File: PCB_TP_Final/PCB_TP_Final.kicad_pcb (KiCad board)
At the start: 2 copper layers, 71 x 135 mm, 20 parts, among them CN10 Conn_02x17_Odd_Even, CN7 Conn_02x10_Odd_Even, CN8 Conn_02x08_Odd_Even, CN9 Conn_02x15_Odd_Even, J1 Conn_01x09, M1 POWER_MB_V2, SW1 SW_Push, U1 NODEMCU_ESP12

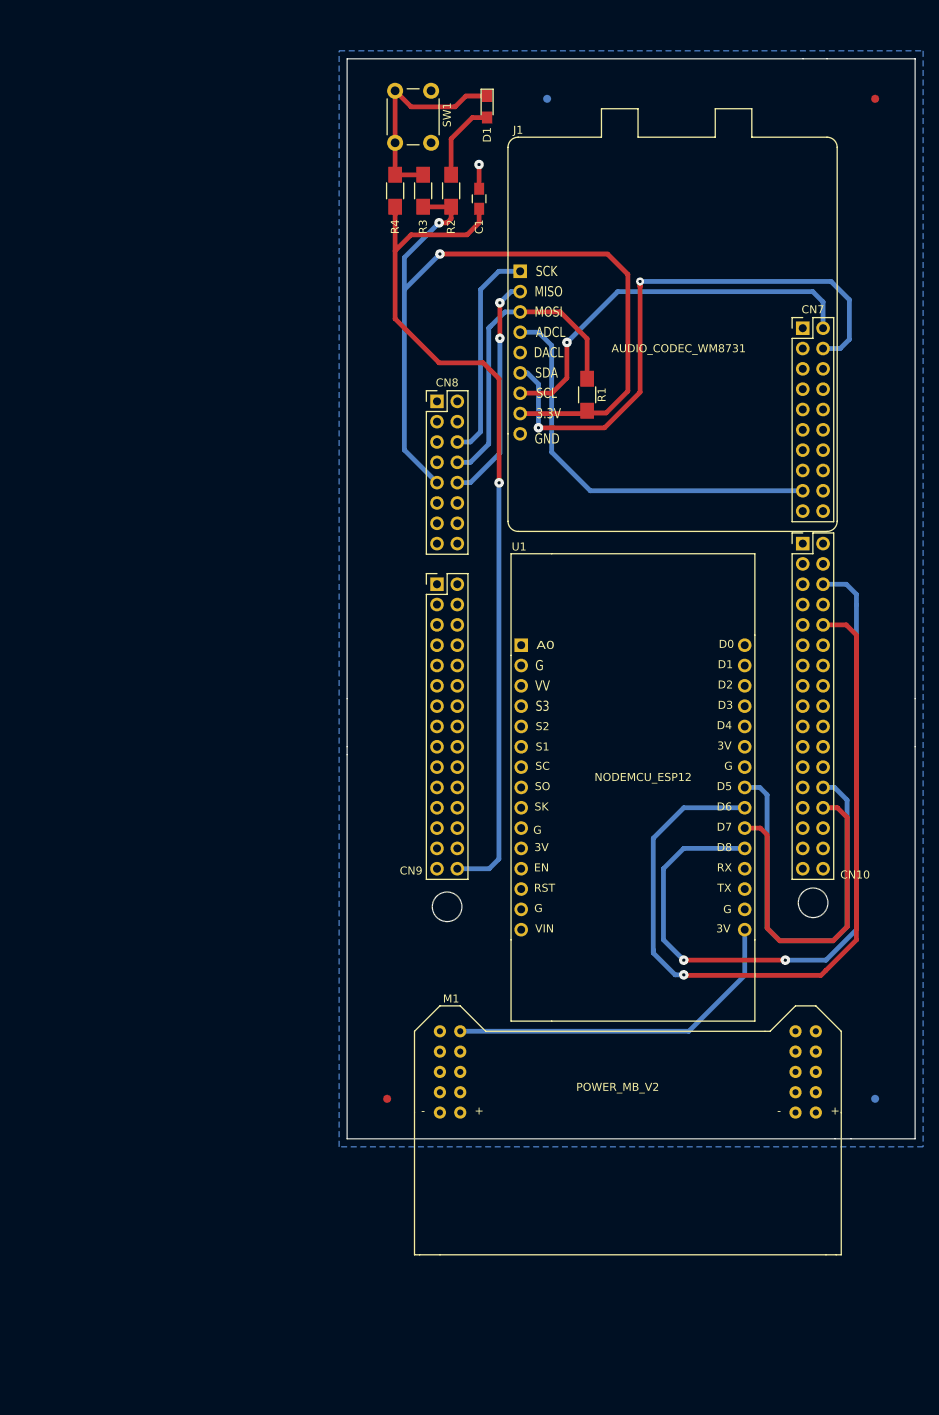
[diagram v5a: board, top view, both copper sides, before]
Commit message: Se agregaron correcciones sugeridas
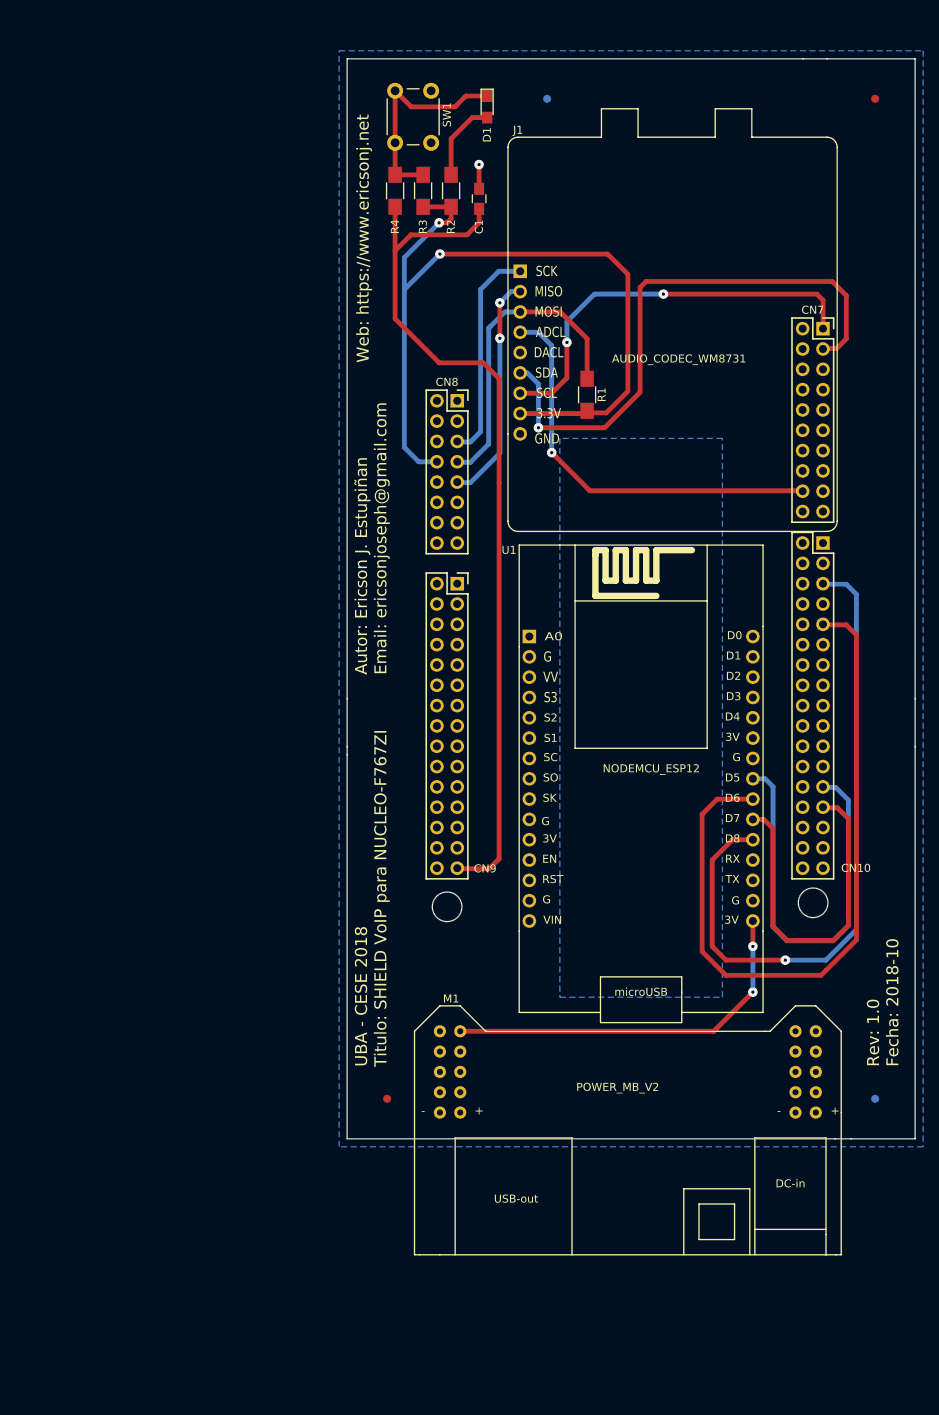
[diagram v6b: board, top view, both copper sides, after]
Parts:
- CN10: footprint Connector_PinHeader_2.54mm:PinHeader_2x17_P2.54mm_Vertical -> Pin_Headers:Pin_Header_Straight_2x17_Pitch2.54mm; moved to B.Cu
- CN7: footprint Connector_PinHeader_2.54mm:PinHeader_2x10_P2.54mm_Vertical -> Pin_Headers:Pin_Header_Straight_2x10_Pitch2.54mm; moved to B.Cu
- CN8: footprint Connector_PinHeader_2.54mm:PinHeader_2x08_P2.54mm_Vertical -> Pin_Headers:Pin_Header_Straight_2x08_Pitch2.54mm; moved to B.Cu
- CN9: footprint Connector_PinHeader_2.54mm:PinHeader_2x15_P2.54mm_Vertical -> Pin_Headers:Pin_Header_Straight_2x15_Pitch2.54mm; moved to B.Cu
- moved CN9 2.53 mm to (117.3, 88.6), turned to 180 degrees
- moved CN10 2.53 mm to (163.0, 83.5), turned to 180 degrees
- moved CN8 2.53 mm to (117.3, 65.8), turned to 180 degrees
- moved CN7 2.53 mm to (163.0, 56.7), turned to 180 degrees
- moved U1 1.15 mm to (140.9, 113.0)
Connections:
- CN10 pad 10: /NODEMCU_ESP12/HMISO -> Net-(CN10-Pad10)
- CN10 pad 25: Net-(CN10-Pad25) -> /NODEMCU_ESP12/HSCLK
- CN10 pad 26: /NODEMCU_ESP12/HSCLK -> Net-(CN10-Pad26)
- CN10 pad 27: Net-(CN10-Pad27) -> /NODEMCU_ESP12/HMOSI
- CN10 pad 28: /NODEMCU_ESP12/HMOSI -> Net-(CN10-Pad28)
- CN10 pad 5: Net-(CN10-Pad5) -> /NODEMCU_ESP12/HCS
- CN10 pad 6: /NODEMCU_ESP12/HCS -> Net-(CN10-Pad6)
- CN10 pad 9: Net-(CN10-Pad9) -> /NODEMCU_ESP12/HMISO
- CN7 pad 1: Net-(CN7-Pad1) -> /AUDIO_CODEC/SCL
- CN7 pad 17: /AUDIO_CODEC/ADCL -> Net-(CN7-Pad17)
- CN7 pad 18: Net-(CN7-Pad18) -> /AUDIO_CODEC/ADCL
- CN7 pad 2: /AUDIO_CODEC/SCL -> Net-(CN7-Pad2)
- CN7 pad 3: Net-(CN7-Pad3) -> /AUDIO_CODEC/SDA
- CN7 pad 4: /AUDIO_CODEC/SDA -> Net-(CN7-Pad4)
- CN8 pad 10: /AUDIO_CODEC/MISO -> Net-(CN8-Pad10)
- CN8 pad 11: GND -> Net-(CN8-Pad11)
- CN8 pad 12: Net-(CN8-Pad12) -> GND
- CN8 pad 13: GND -> Net-(CN8-Pad13)
- CN8 pad 14: Net-(CN8-Pad14) -> GND
- CN8 pad 5: Net-(CN8-Pad5) -> /AUDIO_CODEC/SCK
- CN8 pad 6: /AUDIO_CODEC/SCK -> Net-(CN8-Pad6)
- CN8 pad 7: Net-(CN8-Pad7) -> /AUDIO_CODEC/MOSI
- CN8 pad 8: /AUDIO_CODEC/MOSI -> +3.3VA
- CN8 pad 9: 3.3VB -> /AUDIO_CODEC/MISO
- CN9 pad 11: Net-(CN9-Pad11) -> GND
- CN9 pad 12: GND -> Net-(CN9-Pad12)
- CN9 pad 29: Net-(CN9-Pad29) -> /TalkButton/talk
- CN9 pad 30: /TalkButton/talk -> Net-(CN9-Pad30)
- J1 pad 8: 3.3VB -> +3.3VA
- R1 pad 2: 3.3VB -> +3.3VA
- R2 pad 2: 3.3VB -> +3.3VA
- R3 pad 2: 3.3VB -> +3.3VA
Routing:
- net 3.3VB: track 103.1 -> 0.00 mm, vias 2 -> 0
- net +3.3VA: track 0.00 -> 102.0 mm, vias 0 -> 2
- net /NODEMCU_ESP12/HCS: track 93.5 -> 83.9 mm, vias 2 -> 1
- net /NODEMCU_ESP12/HMISO: track 98.5 -> 89.5 mm, vias 1 -> 0
- net +3V3: track 44.2 -> 47.5 mm, vias 0 -> 2
- net /AUDIO_CODEC/SDA: track 73.2 -> 71.6 mm, vias 2 -> 1
- net /AUDIO_CODEC/SCL: track 49.5 -> 50.9 mm, vias 1 -> 2
- net /TalkButton/talk: track 110.6 -> 110.5 mm, vias 1 -> 0
- net /AUDIO_CODEC/ADCL: track 51.3 -> 51.4 mm, vias 0 -> 1
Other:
- board text added: "Autor: Ericson J. Estupiñan Email: ericsonjoseph@gmail.com"
- board text added: "Rev: 1.0 Fecha: 2018-10"
- board text added: "UBA - CESE 2018 Titulo: SHIELD VoIP para NUCLEO-F767ZI"
- board text added: "Web: https://www.ericsonj.net"

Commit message: Versión lista para revisión
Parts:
- moved F2 0.07 mm to (128.4, 28.0)
- moved F4 0.05 mm to (169.5, 28.0)
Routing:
- net /AUDIO_CODEC/MISO: track 28.8 -> 29.2 mm, vias 2 -> 1
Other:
- board text added: "Minimos (Mayer 5 mils): Grillas: 0.1270mm, 0.5mm, 0.6350mm, 2.54mm Via 1.2mm, 0.6mm: Margen: 0.4mm Pista: 0.6mm Dist. a borde: 0.6mm Terminación: HASL"
- board text removed: "Minimos (Mayer 100 mils): Grillas: 0.1270mm, 0.5mm, 0.6350mm, 2.54mm Via 1.2mm, 0.6mm: Margen: 0.4mm Pista: 0.6mm Dist. a borde: 0.6mm Terminación: HASL"
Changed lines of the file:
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@@
     (area 103.449999 22.949999 174.550001 158.050001)
     (thickness 1.6)
-    (drawings 52)
+    (drawings 51)
     (tracks 156)
     (zones 0)
@@
   )
   (module Fiducials:Fiducial_1mm_Dia_2.54mm_Outer_CopperBottom (layer F.Cu)
-    (at 128.5 28)
+    (at 128.439 28.032)
     (descr "Circular Fiducial, 1mm bare copper bottom; 2.54mm keepout")
     (tags marker)
@@
   )
   (module Fiducials:Fiducial_1mm_Dia_2.54mm_Outer_CopperTop (layer F.Cu)
-    (at 169.5 28)
+    (at 169.46 28.032)
     (descr "Circular Fiducial, 1mm bare copper top; 2.54mm keepout")
     (tags marker)
@@
       (effects (font (size 1 1) (thickness 0.15)))
     )
-    (fp_text value Conn_02x08_Odd_Even (at 1.27 -20.11 180) (layer B.Fab)
+    (fp_text value Conn_02x08_Odd_Even (at 5.334 -9.144 270) (layer B.Fab)
       (effects (font (size 1 1) (thickness 0.15)) (justify mirror))
     )
@@
       (effects (font (size 1 1) (thickness 0.15)))
     )
-    (fp_text value Conn_02x15_Odd_Even (at 1.27 -37.89 180) (layer B.Fab)
+    (fp_text value Conn_02x15_Odd_Even (at 5.334 -17.018 270) (layer B.Fab)
       (effects (font (size 1 1) (thickness 0.15)) (justify mirror))
     )
@@
       (effects (font (size 1 1) (thickness 0.15)))
     )
-    (fp_text value Conn_02x10_Odd_Even (at 1.27 -25.19 180) (layer B.Fab)
+    (fp_text value Conn_02x10_Odd_Even (at 5.334 -10.795 270) (layer B.Fab)
       (effects (font (size 1 1) (thickness 0.15)) (justify mirror))
     )
@@
       (effects (font (size 1 1) (thickness 0.15)))
     )
-    (fp_text value Conn_02x17_Odd_Even (at 1.27 -42.97 180) (layer B.Fab)
+    (fp_text value Conn_02x17_Odd_Even (at 5.334 -14.732 270) (layer B.Fab)
       (effects (font (size 1 1) (thickness 0.15)) (justify mirror))
     )
@@
   (gr_line (start 115.993 64.4175) (end 115.993 67.021) (angle 90) (layer F.SilkS) (width 0.2))
   (gr_line (start 113.3895 64.4175) (end 115.993 64.4175) (angle 90) (layer F.SilkS) (width 0.2))
-  (dimension 48.26 (width 0.3) (layer Dwgs.User)
-    (gr_text "48.260 mm" (at 138.726 136.363) (layer Dwgs.User)
-      (effects (font (size 1.5 1.5) (thickness 0.3)))
-    )
-    (feature1 (pts (xy 162.983 124.298) (xy 162.983 140.968)))
-    (feature2 (pts (xy 114.723 124.298) (xy 114.723 140.968)))
-    (crossbar (pts (xy 114.723 138.268) (xy 162.983 138.268)))
-    (arrow1a (pts (xy 162.983 138.268) (xy 161.856496 138.854421)))
-    (arrow1b (pts (xy 162.983 138.268) (xy 161.856496 137.681579)))
-    (arrow2a (pts (xy 114.723 138.268) (xy 115.849504 138.854421)))
-    (arrow2b (pts (xy 114.723 138.268) (xy 115.849504 137.681579)))
-  )
   (gr_text "Rev: 1.0\nFecha: 2018-10" (at 170.5 149 90) (layer F.SilkS)
     (effects (font (size 1.5 1.5) (thickness 0.3)) (justify left))
@@
     (effects (font (size 1.5 1.5) (thickness 0.3)) (justify left))
   )
-  (gr_text "Minimos (Mayer 100 mils):\nGrillas: 0.1270mm, 0.5mm, 0.6350mm, 2.54mm\nVia 1.2mm, 0.6mm:\nMargen: 0.4mm\nPista: 0.6mm\nDist. a borde: 0.6mm\nTerminación: HASL" (at 177.2705 31.6515) (layer Dwgs.User)
+  (gr_text "Minimos (Mayer 5 mils):\nGrillas: 0.1270mm, 0.5mm, 0.6350mm, 2.54mm\nVia 1.2mm, 0.6mm:\nMargen: 0.4mm\nPista: 0.6mm\nDist. a borde: 0.6mm\nTerminación: HASL" (at 177.2705 31.6515) (layer Dwgs.User)
     (effects (font (size 1.5 1.5) (thickness 0.3)) (justify left))
   )
@@
   (via (at 154.22 139.665) (size 1.2) (drill 0.4) (layers F.Cu B.Cu) (net 79))
   (segment (start 149.325 144.56) (end 154.22 139.665) (width 0.6) (layer F.Cu) (net 79))
-  (segment (start 123.99 52.104) (end 125.133 52.104) (width 0.6) (layer B.Cu) (net 80))
+  (segment (start 122.593 53.501) (end 122.593 52.928) (width 0.6) (layer F.Cu) (net 80))
+  (via (at 122.597 57.9405) (size 1.2) (drill 0.4) (layers F.Cu B.Cu) (net 80))
+  (segment (start 122.597 57.9405) (end 122.593 57.9365) (width 0.6) (layer F.Cu) (net 80))
+  (segment (start 122.593 53.501) (end 122.593 57.9365) (width 0.6) (layer F.Cu) (net 80))
+  (segment (start 123.417 52.104) (end 125.133 52.104) (width 0.6) (layer F.Cu) (net 80))
+  (segment (start 122.593 52.928) (end 123.417 52.104) (width 0.6) (layer F.Cu) (net 80))
   (segment (start 122.597 57.9405) (end 122.597 72.293) (width 0.6) (layer B.Cu) (net 80))
   (segment (start 118.91 75.98) (end 117.27424 75.98) (width 0.6) (layer B.Cu) (net 80))
   (segment (start 122.597 72.293) (end 118.91 75.98) (width 0.6) (layer B.Cu) (net 80))
   (segment (start 122.597 57.9405) (end 122.550002 57.987498) (width 0.6) (layer B.Cu) (net 80))
-  (via (at 122.597 57.9405) (size 1.2) (drill 0.4) (layers F.Cu B.Cu) (net 80))
-  (segment (start 122.593 57.9365) (end 122.597 57.9405) (width 0.6) (layer F.Cu) (net 80))
-  (segment (start 122.593 53.501) (end 122.593 57.9365) (width 0.6) (layer F.Cu) (net 80))
-  (segment (start 122.593 53.501) (end 123.99 52.104) (width 0.6) (layer B.Cu) (net 80))
-  (via (at 122.593 53.501) (size 1.2) (drill 0.4) (layers F.Cu B.Cu) (net 80))
   (segment (start 151.68 120.615) (end 154.22 120.615) (width 0.6) (layer F.Cu) (net 111))
   (segment (start 149.14 123.155) (end 151.68 120.615) (width 0.6) (layer F.Cu) (net 111))

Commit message: para fabricar
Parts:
- added R5: 10K, Resistors_SMD:R_1206_HandSoldering, F.Cu at (146.7, 122.0)
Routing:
- net /NODEMCU_ESP12/HMOSI: track 43.2 -> 52.4 mm
- net /NODEMCU_ESP12/HMISO: track 89.5 -> 94.7 mm
- net GND: track 3.03 -> 7.25 mm, vias 1 -> 2
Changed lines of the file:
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@@
 (kicad_pcb (version 4) (host pcbnew 4.0.7)
   (general
-    (links 31)
+    (links 33)
     (no_connects 0)
-    (area 103.449999 22.949999 174.550001 158.050001)
+    (area 88.435716 22 232.270495 176.700001)
     (thickness 1.6)
     (drawings 51)
-    (tracks 156)
+    (tracks 164)
     (zones 0)
-    (modules 20)
+    (modules 21)
     (nets 133)
   )
@@
     (visible_elements FFFFFFFF)
     (pcbplotparams
-      (layerselection 0x00030_80000001)
+      (layerselection 0x3ffff_80000001)
       (usegerberextensions false)
       (excludeedgelayer true)
@@
       (outputformat 1)
       (mirror false)
-      (drillshape 1)
+      (drillshape 0)
       (scaleselection 1)
       (outputdirectory ""))
@@
     )
   )
+  (module Resistors_SMD:R_1206_HandSoldering (layer F.Cu)
+    (at 146.727 122.012 270)
+    (descr "Resistor SMD 1206, hand soldering")
+    (tags "resistor 1206")
+    (attr smd)
+    (fp_text reference R5 (at -4.572 0.127 270) (layer F.SilkS)
+      (effects (font (size 1 1) (thickness 0.15)))
+    )
+    (fp_text value 10K (at 0 1.9 270) (layer F.Fab)
+      (effects (font (size 1 1) (thickness 0.15)))
+    )
+    (fp_text user %R (at 0 0 270) (layer F.Fab)
+      (effects (font (size 0.7 0.7) (thickness 0.105)))
+    )
+    (fp_line (start -1.6 0.8) (end -1.6 -0.8) (layer F.Fab) (width 0.1))
+    (fp_line (start 1.6 0.8) (end -1.6 0.8) (layer F.Fab) (width 0.1))
+    (fp_line (start 1.6 -0.8) (end 1.6 0.8) (layer F.Fab) (width 0.1))
+    (fp_line (start -1.6 -0.8) (end 1.6 -0.8) (layer F.Fab) (width 0.1))
+    (fp_line (start 1 1.07) (end -1 1.07) (layer F.SilkS) (width 0.12))
+    (fp_line (start -1 -1.07) (end 1 -1.07) (layer F.SilkS) (width 0.12))
+    (fp_line (start -3.25 -1.11) (end 3.25 -1.11) (layer F.CrtYd) (width 0.05))
+    (fp_line (start -3.25 -1.11) (end -3.25 1.1) (layer F.CrtYd) (width 0.05))
+    (fp_line (start 3.25 1.1) (end 3.25 -1.11) (layer F.CrtYd) (width 0.05))
+    (fp_line (start 3.25 1.1) (end -3.25 1.1) (layer F.CrtYd) (width 0.05))
+    (pad 1 smd rect (at -2 0 270) (size 2 1.7) (layers F.Cu F.Paste F.Mask)
+      (net 114 /NODEMCU_ESP12/HMOSI))
+    (pad 2 smd rect (at 2 0 270) (size 2 1.7) (layers F.Cu F.Paste F.Mask)
+      (net 19 GND))
+    (model ${KISYS3DMOD}/Resistors_SMD.3dshapes/R_1206.wrl
+      (at (xyz 0 0 0))
+      (scale (xyz 1 1 1))
+      (rotate (xyz 0 0 0))
+    )
+  )
   (gr_line (start 159.1095 125.5045) (end 159.1095 82.1975) (angle 90) (layer F.SilkS) (width 0.2))
   (gr_line (start 164.3165 125.5045) (end 159.1095 125.5045) (angle 90) (layer F.SilkS) (width 0.2))
@@
   (gr_line (start 103.5 109) (end 103.5 103) (angle 90) (layer Edge.Cuts) (width 0.1))
   (gr_line (start 174.5 109) (end 174.5 103) (angle 90) (layer Edge.Cuts) (width 0.1))
+  (segment (start 146.727 124.012) (end 146.727 128.235) (width 0.6) (layer F.Cu) (net 19))
+  (via (at 146.727 128.235) (size 1.2) (drill 0.4) (layers F.Cu B.Cu) (net 19))
   (segment (start 120 39.25) (end 120 36.23) (width 0.6) (layer F.Cu) (net 19))
   (via (at 119.9935 36.2235) (size 1.2) (drill 0.4) (layers F.Cu B.Cu) (net 19))
@@
   (segment (start 167.17 89.95) (end 165.9 88.68) (width 0.6) (layer B.Cu) (net 111))
   (segment (start 162.99424 88.68) (end 165.9 88.68) (width 0.6) (layer B.Cu) (net 111))
-  (segment (start 162.7305 137.5695) (end 150.8545 137.5695) (width 0.6) (layer F.Cu) (net 112))
+  (segment (start 150.918 137.5695) (end 150.6005 137.5695) (width 0.6) (layer F.Cu) (net 112))
+  (segment (start 149.775 115.535) (end 154.22 115.535) (width 0.6) (layer F.Cu) (net 112))
+  (segment (start 146.219 115.535) (end 149.775 115.535) (width 0.6) (layer F.Cu) (net 112))
+  (segment (start 144.314 117.44) (end 146.219 115.535) (width 0.6) (layer F.Cu) (net 112))
+  (segment (start 144.314 131.283) (end 144.314 117.44) (width 0.6) (layer F.Cu) (net 112))
+  (segment (start 150.6005 137.5695) (end 144.314 131.283) (width 0.6) (layer F.Cu) (net 112))
+  (segment (start 162.7305 137.5695) (end 150.918 137.5695) (width 0.6) (layer F.Cu) (net 112))
+  (segment (start 150.918 137.5695) (end 150.8545 137.5695) (width 0.6) (layer F.Cu) (net 112))
   (segment (start 163.36 136.94) (end 167.17 133.13) (width 0.6) (layer F.Cu) (net 112))
   (segment (start 162.7305 137.5695) (end 163.36 136.94) (width 0.6) (layer F.Cu) (net 112))
-  (segment (start 149.775 115.535) (end 154.22 115.535) (width 0.6) (layer F.Cu) (net 112))
-  (segment (start 147.87 117.44) (end 149.775 115.535) (width 0.6) (layer F.Cu) (net 112))
-  (segment (start 147.87 134.585) (end 147.87 117.44) (width 0.6) (layer F.Cu) (net 112))
-  (segment (start 150.8545 137.5695) (end 147.87 134.585) (width 0.6) (layer F.Cu) (net 112))
   (segment (start 167.17 133.13) (end 167.17 95.03) (width 0.6) (layer F.Cu) (net 112))
   (segment (start 167.17 95.03) (end 165.9 93.76) (width 0.6) (layer F.Cu) (net 112))
@@
   (segment (start 164.58 114.08) (end 166.169998 115.669998) (width 0.6) (layer B.Cu) (net 113))
   (segment (start 162.99424 114.08) (end 164.58 114.08) (width 0.6) (layer B.Cu) (net 113))
+  (segment (start 146.727 120.012) (end 146.727 118.456) (width 0.6) (layer F.Cu) (net 114))
+  (segment (start 147.108 118.075) (end 154.22 118.075) (width 0.6) (layer F.Cu) (net 114))
+  (segment (start 146.727 118.456) (end 147.108 118.075) (width 0.6) (layer F.Cu) (net 114))
   (segment (start 155.575 118.075) (end 154.22 118.075) (width 0.6) (layer F.Cu) (net 114))
   (segment (start 156.7 119.2) (end 155.575 118.075) (width 0.6) (layer F.Cu) (net 114))
@@
     )
     (polygon
-      (pts        (xy 130.09 70.45) (xy 130.09 140.3) (xy 150.41 140.3) (xy 150.41 70.45)
+      (pts        (xy 130.09 77.689) (xy 130.09 114.773) (xy 150.41 114.773) (xy 150.41 77.689)
       )
     )
